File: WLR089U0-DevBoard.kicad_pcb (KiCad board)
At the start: 2 copper layers, 29.9 x 40.1 mm, 23 parts, among them IC1 WLR089U0-I_RM, J1 USB_B_Micro, J2 Conn_ARM_JTAG_SWD_10, J3 Conn_01x10_Female, J4 Conn_01x02_Male, J5 Conn_01x10_Female, J6 Conn_01x08_Male, SW1 SW_Push, U1 MCP1700-3302E_SOT23, U2 CH304E

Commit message: labeling done
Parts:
- SWD : renamed from J2
- moved Reset 1.97 mm to (124.2, 77.5)
- moved R1 1.60 mm to (130.1, 75.0), turned to 180 degrees
- renumbered TP1 to +3v, TP2 to GND, D2 to PA08, SW1 to Reset, JP1 to uart_D+, JP2 to uart_D-, U2 to usb_uart, JP3 to usb_uart_vcc
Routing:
- net RESET: track 50.9 -> 53.0 mm
- net +3V3: track 90.4 -> 89.2 mm
- net GND: track 47.5 -> 48.3 mm
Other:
- board text added: "+3V"
- board text added: "3V"
- board text added: "5V"
- board text added: "Current_test"
- board text added: "GND"
- board text added: "I2C_SCL_PA17"
- board text added: "I2C_SDA_PA16"
- board text added: "LED"
- board text added: "MISO_PB02"
- board text added: "MOSI_PB22"
- board text added: "PA06"
- board text added: "PA07"
- board text added: "PA08"
- board text added: "PA14"
- board text added: "PA15"
- board text added: "PA18"
- board text added: "PA19"
- board text added: "PA22"
- board text added: "PA27"
- board text added: "PA28"
- board text added: "PB03"
- board text added: "RX_PA05"
- board text added: "SCK_PB23"
- board text added: "SS_PA23"
- board text added: "SWDCLK"
- board text added: "SWDIO"
- board text added: "TX_PA04"
- board text added: "USB_micro_B"
- board text added: "VDDCORE"
- board text added: "VSW"
- board text added: "WLR089U0-I_RM"

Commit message: editing
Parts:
- added C4: 100n, Capacitor_SMD:C_0402_1005Metric_Pad0.74x0.62mm_HandSolder, F.Cu at (116.3, 76.9)
- added C5: 100n, Capacitor_SMD:C_0402_1005Metric_Pad0.74x0.62mm_HandSolder, F.Cu at (115.0, 78.5)
- added R4: 4.7k, Resistor_SMD:R_1206_3216Metric_Pad1.42x1.75mm_HandSolder, F.Cu at (134.1, 106.7)
- added R5: 4.7k, Resistor_SMD:R_1206_3216Metric_Pad1.42x1.75mm_HandSolder, F.Cu at (129.1, 106.8)
- J2: renamed from SWD 
- moved uart_D- 9.71 mm to (109.6, 107.5)
- moved C2 7.68 mm to (123.8, 106.8), turned to 180 degrees
- moved C3 6.80 mm to (118.8, 105.5)
- moved R2 3.08 mm to (132.2, 103.1), turned to 180 degrees
- moved D1 2.84 mm to (127.2, 103.3)
- moved U1 2.46 mm to (123.5, 103.9)
- moved C1 1.02 mm to (118.9, 103.1)
- moved J2 1.02 mm to (127.1, 111.2)
- moved uart-D+ 0.78 mm to (108.5, 103.9)
- moved J4 0.64 mm to (122.3, 110.2)
- moved Usb_uart 0.58 mm to (110.1, 100.6)
- moved TP2 0.54 mm to (109.2, 110.3)
- moved U2 0.38 mm to (113.2, 104.2)
- renumbered PA08 to D2, Reset to SW1, +3v to TP1, GND to TP2, usb_uart to U2, usb_uart_vcc to Usb_uart, uart_D+ to uart-D+
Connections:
- J2 pad 6: (no net) -> Net-(J2-Pad6)
- J2 pad 7: (no net) -> Net-(J2-Pad7)
- J2 pad 8: (no net) -> Net-(J2-Pad8)
- U2 pad 4: (no net) -> Net-(U2-Pad4)
- U2 pad 5: (no net) -> Net-(U2-Pad5)
- U2 pad 6: (no net) -> Net-(U2-Pad6)
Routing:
- net +3V3: track 89.2 -> 0.00 mm
- net +5V: track 58.1 -> 0.00 mm, vias 2 -> 0
- net RESET: track 53.0 -> 0.00 mm
- net GND: track 48.3 -> 0.00 mm, vias 13 -> 0
- net S0_UART_TX: track 40.7 -> 0.00 mm, vias 1 -> 0
- net S0_UART_RX: track 34.6 -> 0.00 mm
- net USB_DP: track 27.1 -> 0.00 mm, vias 2 -> 0
- net SWDCLK: track 25.0 -> 0.00 mm, vias 1 -> 0
- net Net-(C3-Pad1): track 24.3 -> 0.00 mm, vias 2 -> 0
- net SWDIO: track 23.4 -> 0.00 mm, vias 1 -> 0
- net PA08: track 16.3 -> 0.00 mm
- net USB_DM: track 13.5 -> 0.00 mm, vias 2 -> 0
- net D+: track 13.1 -> 0.00 mm
- net /3V3: track 12.9 -> 0.00 mm
- net PA07: track 9.84 -> 0.00 mm
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
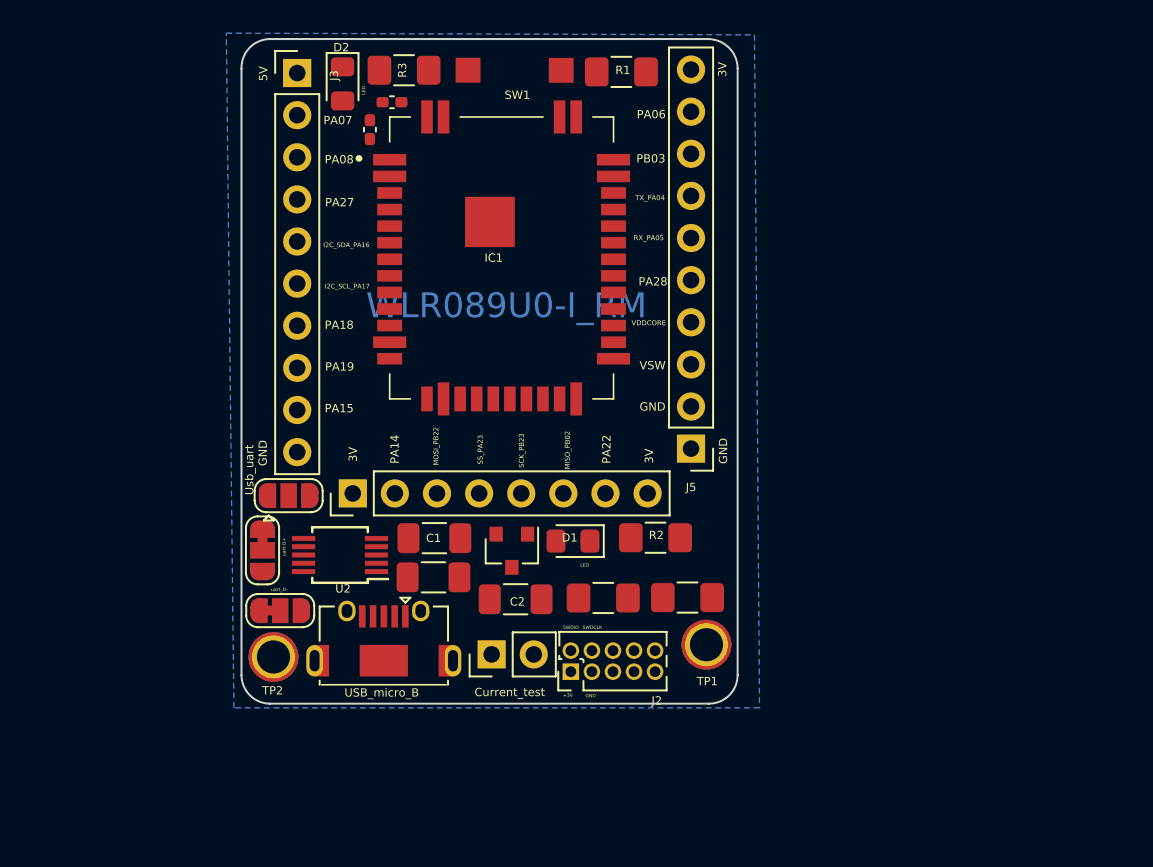
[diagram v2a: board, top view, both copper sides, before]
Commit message: coupling cap placement pending
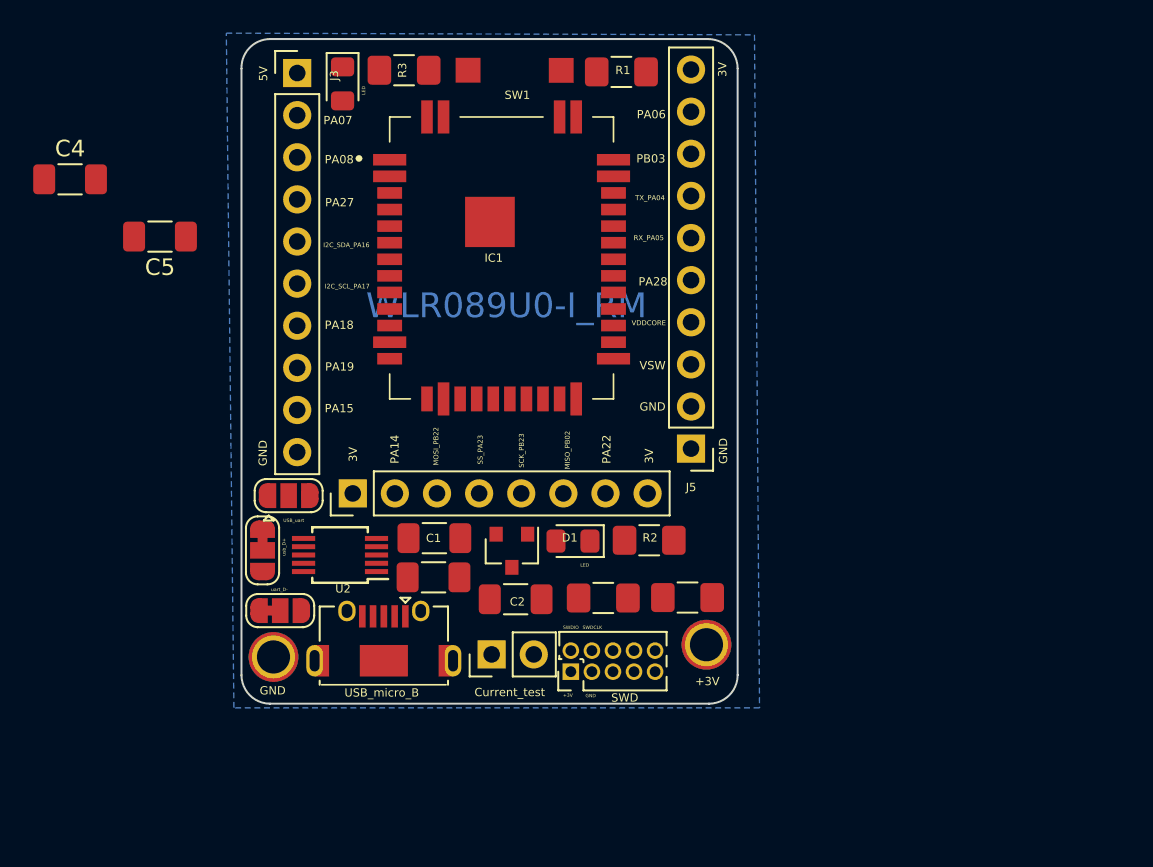
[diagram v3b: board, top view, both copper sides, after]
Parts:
- C4, C5: footprint Capacitor_SMD:C_0402_1005Metric_Pad0.74x0.62mm_HandSolder -> Capacitor_SMD:C_1206_3216Metric_Pad1.33x1.80mm_HandSolder
- moved C4 20.0 mm to (96.9, 81.5)
- moved C5 14.2 mm to (102.3, 85.0), turned to 180 degrees
- moved R2 0.41 mm to (131.8, 103.3)
- renumbered TP1 to +3V, TP2 to GND, J2 to SWD, Usb_uart to USB_uart, uart-D+ to usb_D+

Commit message: Changed orientation, rearranged symbols
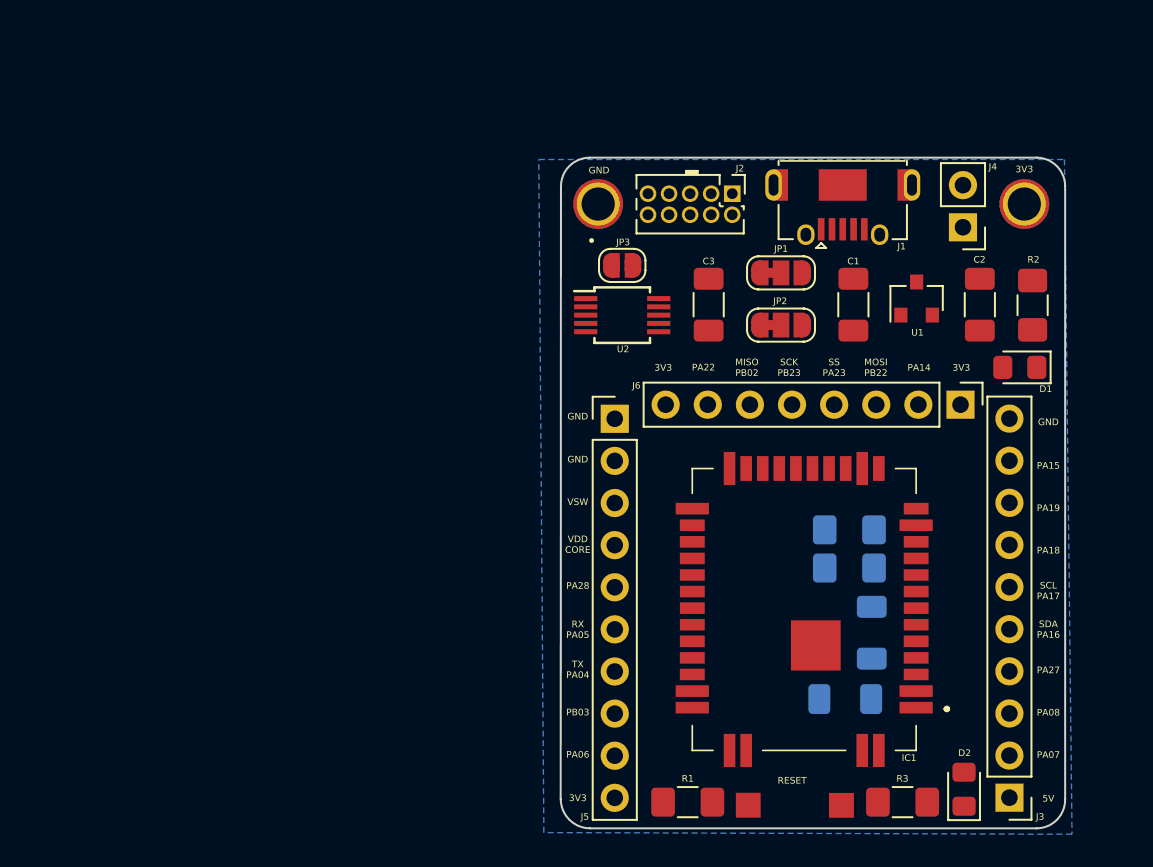
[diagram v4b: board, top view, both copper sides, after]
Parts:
- added G***: LOGO, JithinIsaac_Footprints:KiCad-Logo2_8X4mm_SilkScreen, B.Cu at (135.6, 102.8)
- added G***: LOGO, JithinIsaac_Footprints:OSHW_Logo_4.3x4.5mm, B.Cu at (135.4, 109.2)
- C4, C5, R4, R5: moved to B.Cu
- JP3: renamed from USB_uart; footprint Jumper:SolderJumper-3_P1.3mm_Open_RoundedPad1.0x1.5mm -> Jumper:SolderJumper-2_P1.3mm_Open_RoundedPad1.0x1.5mm
- moved J3 61.3 mm to (153.6, 118.8), turned to 180 degrees
- moved D2 56.7 mm to (150.8, 118.3), turned to 90 degrees
- moved C4 55.5 mm to (145.2, 108.8), turned to 90 degrees
- moved R3 53.4 mm to (147.1, 119.1), turned to 0 degrees
- moved C5 49.9 mm to (143.7, 112.8)
- moved R1 44.2 mm to (134.2, 119.1), turned to 0 degrees
- moved RESET 42.3 mm to (140.1, 116.7), turned to 0 degrees
- moved J1 39.9 mm to (143.5, 81.8), turned to 180 degrees
- moved J4 38.4 mm to (150.8, 84.4), turned to 180 degrees
- moved J6 37.0 mm to (150.6, 95.1), turned to 270 degrees
- moved JP1 35.5 mm to (139.8, 87.2), turned to 0 degrees
- moved JP2 34.8 mm to (139.8, 90.3)
- moved GND 33.6 mm to (128.8, 83.0), turned to 180 degrees
- moved C2 33.2 mm to (151.8, 89.1), turned to 90 degrees
- moved 3V3 32.8 mm to (154.4, 83.0), turned to 180 degrees
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- renumbered +3V to 3V3, SWD to J2, usb_D+ to JP1, uart_D- to JP2, SW1 to RESET
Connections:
- J2 pad 6: Net-(J2-Pad6) -> (no net)
- J2 pad 7: Net-(J2-Pad7) -> (no net)
- J2 pad 8: Net-(J2-Pad8) -> (no net)
- U2 pad 4: Net-(U2-Pad4) -> (no net)
- U2 pad 5: Net-(U2-Pad5) -> (no net)
- U2 pad 6: Net-(U2-Pad6) -> (no net)
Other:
- board size 29.9 x 40.1 mm -> 30.4 x 40.4 mm
- net class Power added: clearance 0.3, trace_width 0.4, via_dia 0.8, via_drill 0.4
- board text added: "3V3"
- board text added: "Atul Kumar, Jithin Saji Isaac DBIT, Mumbai"
- board text added: "MISO PB02"
- board text added: "MOSI PB22"
- board text added: "RX PA05"
- board text added: "SCK PB23"
- board text added: "SCL PA17"
- board text added: "SDA PA16"
- board text added: "SS PA23"
- board text added: "TX PA04"
- board text added: "VDD CORE"
- board text added: "WLR089U0 SAMR34 DEV BOARD"
- board text removed: "+3V"
- board text removed: "3V"
- board text removed: "Current_test"
- board text removed: "I2C_SCL_PA17"
- board text removed: "I2C_SDA_PA16"
- board text removed: "LED"
- board text removed: "MISO_PB02"
- board text removed: "MOSI_PB22"
- board text removed: "RX_PA05"
- board text removed: "SCK_PB23"
- board text removed: "SS_PA23"
- board text removed: "SWDCLK"
- board text removed: "SWDIO"
- board text removed: "TX_PA04"
- board text removed: "USB_micro_B"
- board text removed: "VDDCORE"
- board text removed: "WLR089U0-I_RM"

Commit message: Increased board & SS size, completed layout,routing done. final inspection remains
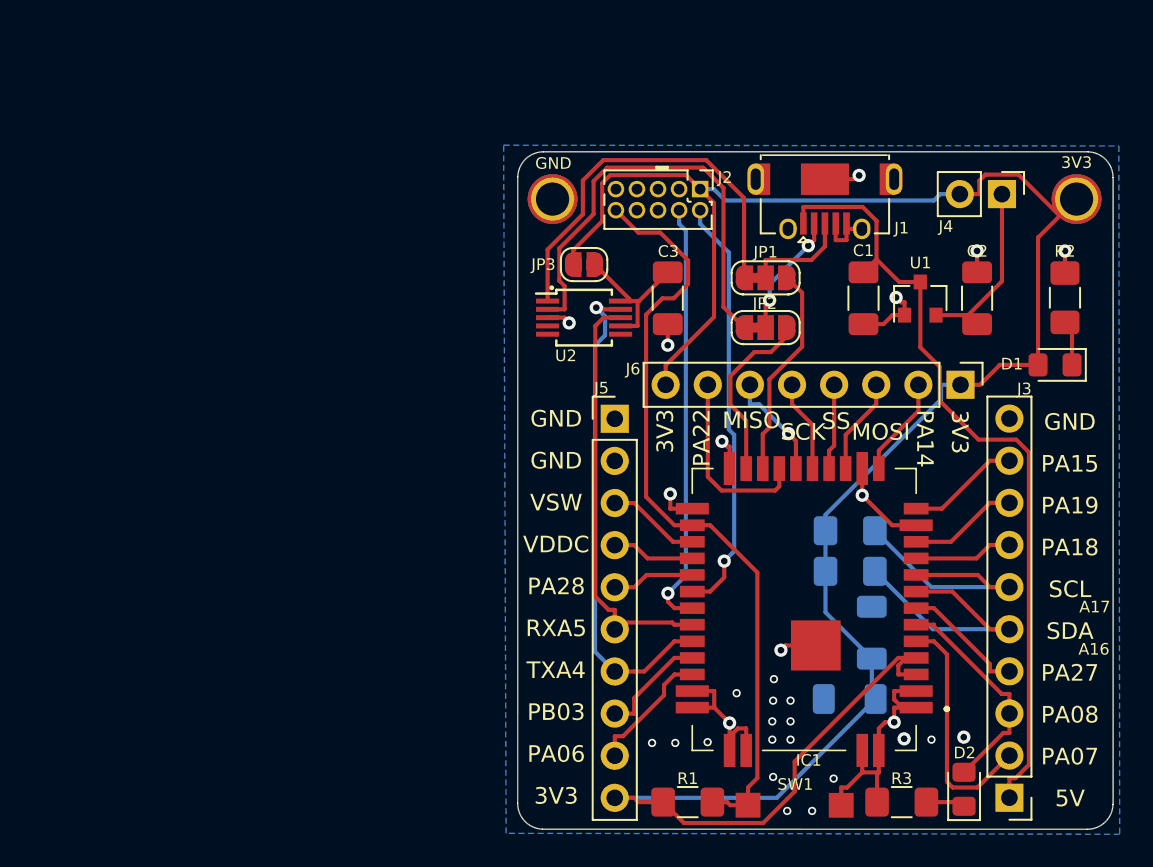
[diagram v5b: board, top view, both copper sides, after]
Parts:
- moved 3V3 3.16 mm to (157.6, 82.7)
- moved J4 3.09 mm to (153.1, 82.4), turned to 270 degrees
- moved GND 2.77 mm to (126.0, 82.7)
- moved C3 2.50 mm to (132.9, 88.7)
- moved U2 2.30 mm to (127.9, 89.8)
- moved JP3 2.30 mm to (127.9, 86.7)
- moved D1 2.13 mm to (156.3, 92.7)
- moved R2 2.00 mm to (156.9, 88.7)
- moved J2 1.95 mm to (134.9, 82.1)
- moved J6 1.20 mm to (150.6, 93.9)
- moved J1 1.13 mm to (142.4, 81.5)
- moved JP1 0.98 mm to (138.8, 87.5)
- moved JP2 0.94 mm to (138.8, 90.5)
- moved C1 0.72 mm to (144.8, 88.7)
- moved C2 0.42 mm to (151.6, 88.7)
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- renumbered G*** to KiCad, RESET to SW1
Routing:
- net +3V3: track 0.00 -> 134.5 mm
- net GND: track 0.00 -> 52.9 mm, vias 0 -> 30
- net +5V: track 0.00 -> 48.2 mm
- net RESET: track 0.00 -> 46.4 mm
- net S0_UART_TX: track 0.00 -> 29.8 mm, vias 0 -> 1
- net Net-(JP2-Pad1): track 0.00 -> 27.4 mm
- net SWDCLK: track 0.00 -> 25.9 mm, vias 0 -> 1
- net SWDIO: track 0.00 -> 25.5 mm, vias 0 -> 1
- net S0_UART_RX: track 0.00 -> 25.5 mm
- net Net-(JP1-Pad1): track 0.00 -> 24.1 mm
- net S1_I2C_SDA: track 0.00 -> 16.1 mm
- net S1_I2C_SCL: track 0.00 -> 15.4 mm
- net PA07: track 0.00 -> 14.6 mm
- net PA08: track 0.00 -> 13.5 mm
- net USB_DP: track 0.00 -> 12.9 mm
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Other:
- board size 30.4 x 40.4 mm -> 35.9 x 40.9 mm
- board text added: "A16"
- board text added: "A17"
- board text added: "Atul Kumar, Jithin Isaac DBIT, Mumbai"
- board text added: "MISO"
- board text added: "MOSI"
- board text added: "RXA5"
- board text added: "SCK"
- board text added: "SCL"
- board text added: "SDA"
- board text added: "SS"
- board text added: "TXA4"
- board text added: "VDDC"
- board text removed: "Atul Kumar, Jithin Saji Isaac DBIT, Mumbai"
- board text removed: "MISO PB02"
- board text removed: "MOSI PB22"
- board text removed: "RX PA05"
- board text removed: "SCK PB23"
- board text removed: "SCL PA17"
- board text removed: "SDA PA16"
- board text removed: "SS PA23"
- board text removed: "TX PA04"
- board text removed: "VDD CORE"
